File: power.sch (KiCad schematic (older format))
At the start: 16 parts, among them J3 USB_B_Micro, Q1 Q_NMOS_GSD, Q2 Q_NMOS_GSD, U2 APE8865U4-33-HF-3, U3 AP9101C, U4 MCP73812T-435I-OT

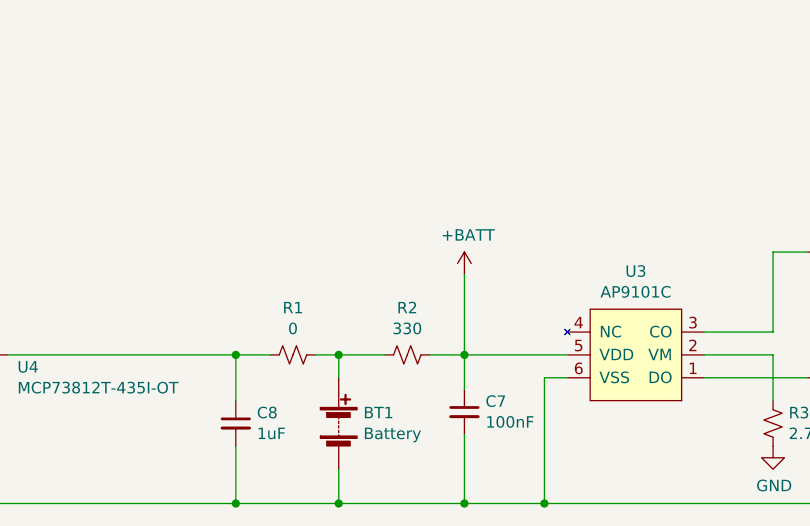
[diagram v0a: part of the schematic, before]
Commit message: DFM version
Add ability for microcontroller to enable/disable backlight, fix bug
with where BATT net comes from, create gerbers to submit to DFM.
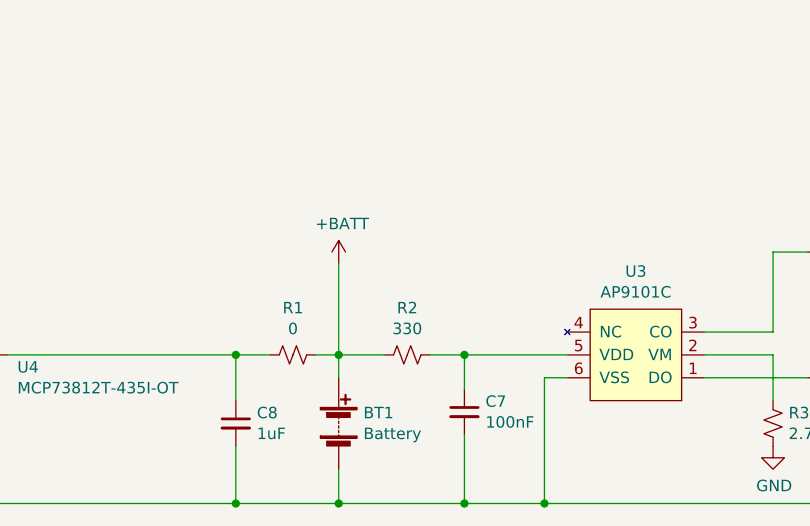
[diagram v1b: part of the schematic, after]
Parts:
- U4: footprint Package_TO_SOT_SMD:SOT-23-5 -> Package_TO_SOT_SMD:SOT-23-5_HandSoldering
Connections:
- net +BATT: now also BT1.1 (+), R1.1, R2.2; no longer C7.1, R2.1, U3.5 (VDD)
- new net: C7.1, R2.1, U3.5 (VDD)
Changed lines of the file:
@@
 EESchema Schematic File Version 4
-LIBS:rpn_mxb-cache
-EELAYER 29 0
+EELAYER 30 0
 EELAYER END
 $Descr A4 11693 8268
@@
 F 0 "U4" H 3744 3646 50  0000 L CNN
 F 1 "MCP73812T-435I-OT" H 3744 3555 50  0000 L CNN
-F 2 "Package_TO_SOT_SMD:SOT-23-5" H 3350 3350 50  0001 L CNN
+F 2 "Package_TO_SOT_SMD:SOT-23-5_HandSoldering" H 3350 3350 50  0001 L CNN
 F 3 "http://ww1.microchip.com/downloads/en/DeviceDoc/22036b.pdf" H 3050 3850 50  0001 C CNN
 	1    3300 3600
@@
 	5150 3500 5350 3500
 Wire Wire Line
-	5550 3500 5700 3500
-Wire Wire Line
 	5700 3650 5700 3500
-Connection ~ 5700 3500
-Wire Wire Line
-	5700 3500 6150 3500
 Wire Wire Line
 	5700 3850 5700 4150
@@
 L power:+BATT #PWR0107
 U 1 1 5D365457
-P 5700 3150
-F 0 "#PWR0107" H 5700 3000 50  0001 C CNN
-F 1 "+BATT" H 5715 3323 50  0000 C CNN
-F 2 "" H 5700 3150 50  0001 C CNN
-F 3 "" H 5700 3150 50  0001 C CNN
-	1    5700 3150
-	1    0    0    -1
-$EndComp
-Wire Wire Line
-	5700 3500 5700 3150
+P 5150 3100
+F 0 "#PWR0107" H 5150 2950 50  0001 C CNN
+F 1 "+BATT" H 5165 3273 50  0000 C CNN
+F 2 "" H 5150 3100 50  0001 C CNN
+F 3 "" H 5150 3100 50  0001 C CNN
+	1    5150 3100
+	1    0    0    -1
+$EndComp
 $Comp
 L power:GND #PWR0108
@@
 	9800 1650 9800 1850
 Connection ~ 9800 1850
+Wire Wire Line
+	5150 3100 5150 3500
+Wire Wire Line
+	5700 3500 6150 3500
+Wire Wire Line
+	5550 3500 5700 3500
+Connection ~ 5700 3500
 $EndSCHEMATC

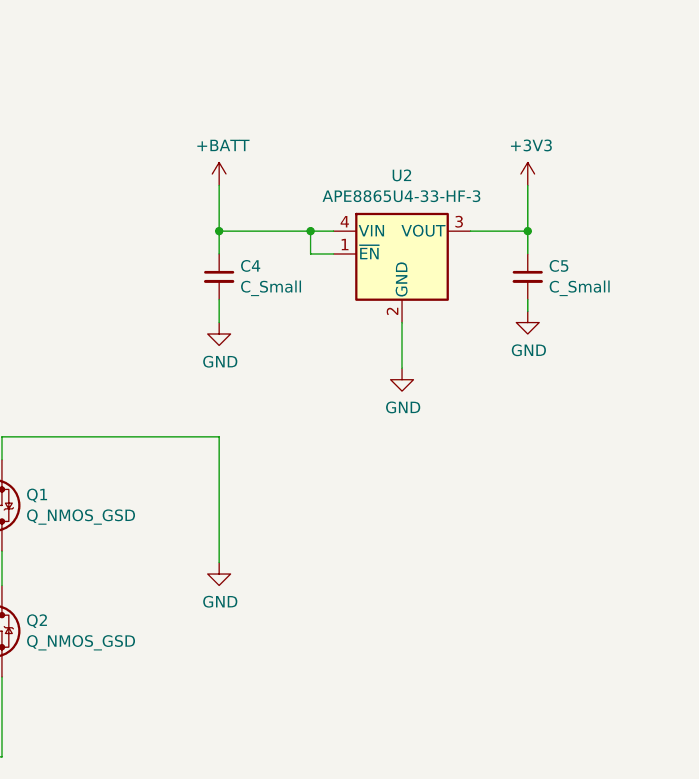
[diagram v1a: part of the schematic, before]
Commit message: Add TODO comments to schematic based on assemby epiphanies
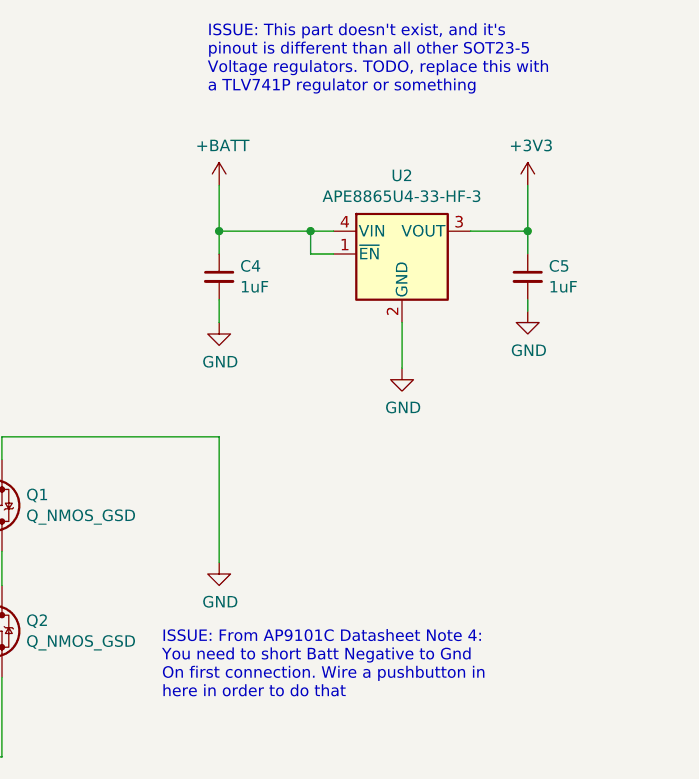
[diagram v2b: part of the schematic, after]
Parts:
- C4, C5: value C_Small -> 1uF
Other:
- note added: "ISSUE: From AP9101C Datasheet Note 4:\nYou need to short Batt Negative to Gnd\nOn first connection. Wire a pushbutton in\nhere in order to do that"
- note added: "ISSUE: This part doesn't exist, and it's\npinout is different than all other SOT23-5\nVoltage regulators. TODO, replace this with\na TLV741P regulator or something"
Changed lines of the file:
@@
 P 9800 2050
 F 0 "C5" H 9892 2096 50  0000 L CNN
-F 1 "C_Small" H 9892 2005 50  0000 L CNN
+F 1 "1uF" H 9892 2005 50  0000 L CNN
 F 2 "Capacitor_SMD:C_0805_2012Metric_Pad1.15x1.40mm_HandSolder" H 9800 2050 50  0001 C CNN
 F 3 "~" H 9800 2050 50  0001 C CNN
@@
 P 8450 2050
 F 0 "C4" H 8542 2096 50  0000 L CNN
-F 1 "C_Small" H 8542 2005 50  0000 L CNN
+F 1 "1uF" H 8542 2005 50  0000 L CNN
 F 2 "Capacitor_SMD:C_0805_2012Metric_Pad1.15x1.40mm_HandSolder" H 8450 2050 50  0001 C CNN
 F 3 "~" H 8450 2050 50  0001 C CNN
@@
 	5550 3500 5700 3500
 Connection ~ 5700 3500
+Text Notes 8200 3900 0    50   ~ 0
+ISSUE: From AP9101C Datasheet Note 4:\nYou need to short Batt Negative to Gnd\nOn first connection. Wire a pushbutton in\nhere in order to do that
+Text Notes 8400 1250 0    50   ~ 0
+ISSUE: This part doesn't exist, and it's\npinout is different than all other SOT23-5\nVoltage regulators. TODO, replace this with\na TLV741P regulator or something
 $EndSCHEMATC
